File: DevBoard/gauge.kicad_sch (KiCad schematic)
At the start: 78 parts, among them J101 Pack (welded 4S) - use instea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, J102 Cell 1 NTC 10k 103AT, J103 EV2400 SMBus, J104 Bench PACK_P, J105 Cell 2 NTC 10k 103AT, J106 Cell 3 NTC 10k 103AT, J107 Cell 4 NTC 10k 103AT, Q101 AGM404AP1, Q102 AGM404AP1, Q103 AO3400A, Q104 AO3400A, SW101 WAKE, U101 BQ40Z50RSMR-R2, U102 BQ294700DSGR

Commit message: Dev board rev A7: CC2340R5MODA MCU, TMP1075 sensors, shared IRQ_N
- U301 STM32WB1MMC -> TI CC2340R5MODA (cost-down; BLE only, on-chip OTA).
  New symbol and footprint (MHA0024A, with the fig. 9-2 antenna keep-out),
  RF match C313/R321/C314/C315, RSTN pull-up R302, wired per SWRS349A fig. 9-1.
- Only 10 usable GPIOs, so the five board NTCs become TMP1075 I2C sensors:
  U302-U304 fitted (port 1 stage, port 2 stage, connectors), U305/U306 DNP.
  FET over-temperature moves to the gauge internal sensor.
- TPS25751 IRQs, gauge BTP and TMP1075 ALERTs share one open-drain IRQ_N
  (R314 pull-up; R315, R114 DNP).
- R313 fitted at 470k: CC2340 pins float in reset, so it keeps the 3V3 rail
  out of sleep mode during boot.
- Pin budget doc, circuit description, bring-up checklist and README item 40
  updated; mcu-io-power-states.md flagged for rewrite. PCB not updated yet.

Co-Authored-By: Claude Opus 5.5 <noreply@anthropic.com>
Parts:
- R114: now not fitted
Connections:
- net GAUGE_BTP renamed IRQ_N
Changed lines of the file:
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@@
 		)
 	)
-	(global_label "GAUGE_BTP"
+	(global_label "IRQ_N"
 		(shape bidirectional)
 		(at 294.64 181.61 270)
@@
 		)
 	)
-	(global_label "GAUGE_BTP"
+	(global_label "IRQ_N"
 		(shape bidirectional)
 		(at 312.42 190.5 270)
@@
 		)
 	)
-	(global_label "GAUGE_BTP"
+	(global_label "IRQ_N"
 		(shape bidirectional)
 		(at 342.9 179.07 90)
@@
 		(on_board yes)
 		(in_pos_files yes)
-		(dnp no)
+		(dnp yes)
 		(property "Reference" "R114"
 			(at 298.87 176.67 0)

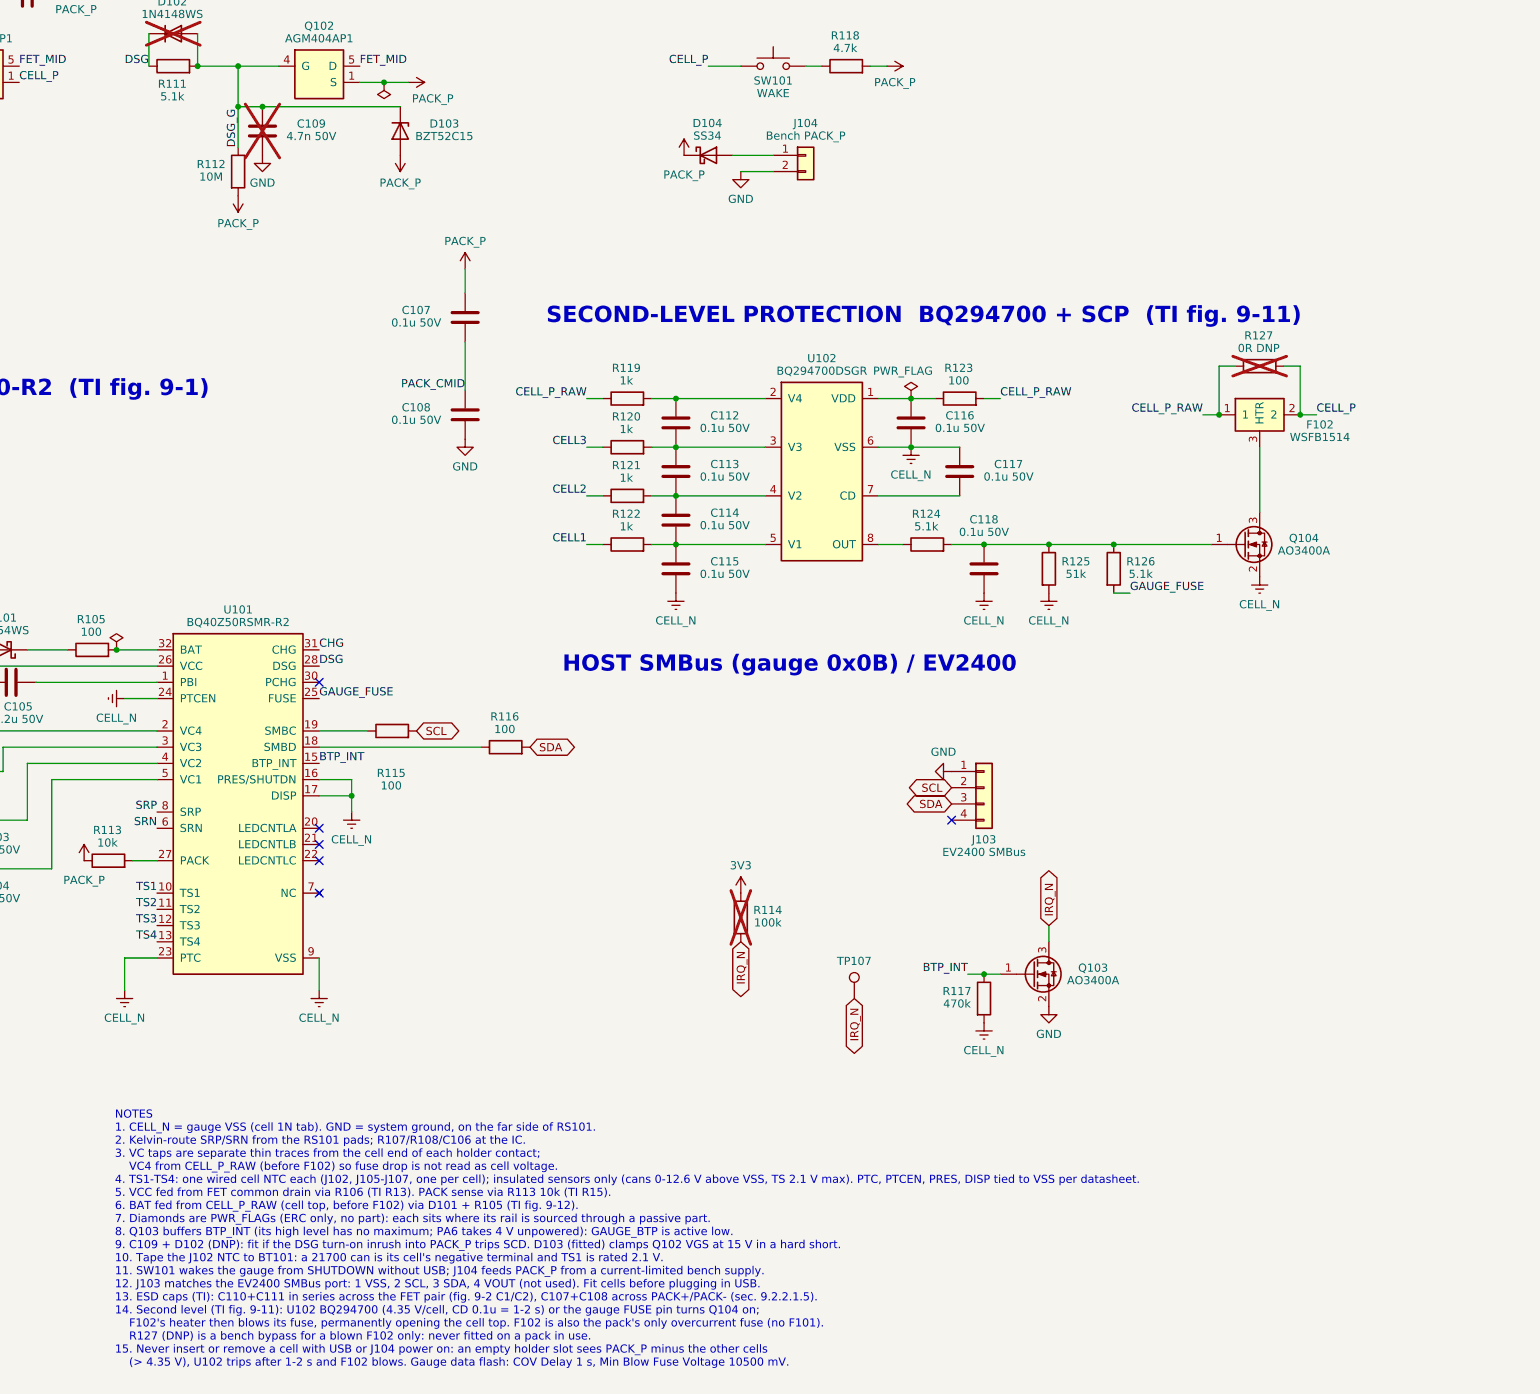
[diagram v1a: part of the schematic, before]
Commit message: Dev board rev A8 part 2: review 4 docs, BOM, A-2 procedure, J104 clamp
Schematic edits by tools/review4_docs.py (helpers split out of
review4_fixes.py into tools/sch_edit.py; review4_fixes output unchanged).
- A-2: EV2400 work only with 3V3 up (J104) and U301 in reset; checklist,
  R312/R301 Notes and MCU sheet note 10 rewritten.
- D-5: D105 SMAJ18A clamp on the J104 side of D104; board placed
  (D104 moved one body width left).
- Stale Notes, sheet notes, heading and address text fixed; sheet 4
  renamed "MCU and Sensors"; revision log A7/A8; title blocks A8.
- MPNs filled on the parts that had only LCSC numbers; Sourcing on U301
  and J301; J301 out of the position file.
- bringup-config-checklist, mcu-io-power-states and power-budget rewritten
  for the CC2340 with every review 4 CONFIG item; corrections in
  circuit-description, cost-down and cc2340-pin-budget.
ERC: 8 known warnings. 0 text overlaps. DRC: 0 parity issues, no
courtyard overlaps (429 parts). README item 42.

Co-Authored-By: Claude Opus 5.5 <noreply@anthropic.com>
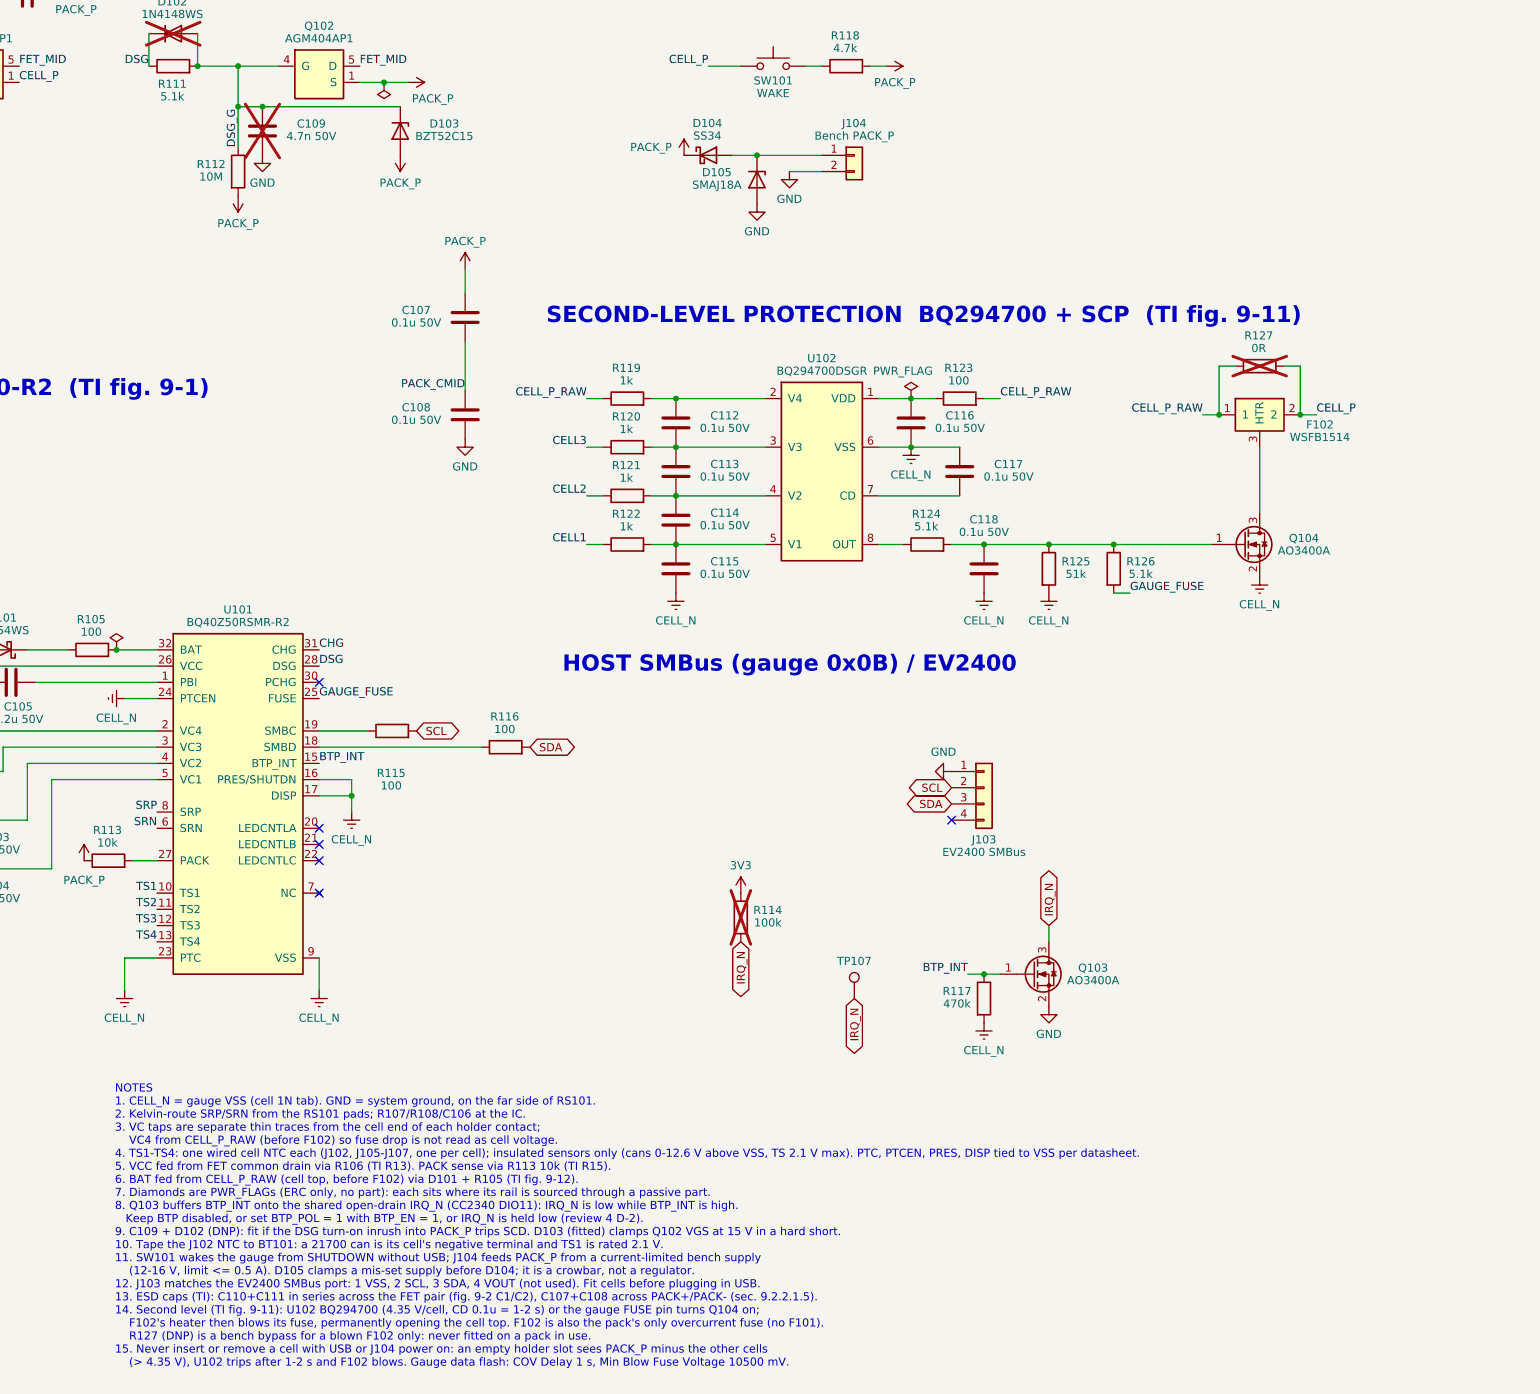
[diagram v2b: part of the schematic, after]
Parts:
- added D105: SMAJ18A, Diode_SMD:D_SMA, symbol Device:D_Zener
- BT101, BT102, BT103, BT104: MPN (none) -> BH-21700-B1BJ001 (MYOUNG)
- D101: MPN (none) -> BAT54WS (R+O)
- J102: Notes Wired 10k B3435 NTC (Semitec 103AT-2 class, epoxy bead with insulated leads) taped to the side of BT101, over its sleeve. The can is that cell's negative terminal (VSS above VSS) and the TS pins are rated 2.1 V: keep the sensor insulated. Gauge internal 18k pull-up; enable TS1 in data flash -> Wired 10k B3435 NTC (Semitec 103AT-2 class, epoxy bead with insulated leads) taped to the side of BT101, over its sleeve. The can is that cell's negative terminal (at VSS) and the TS pins are rated 2.1 V: keep the sensor insulated. Gauge internal 18k pull-up; enable TS1 in data flash
- Q101, Q102: MPN (none) -> AGM404AP1 (AGMSEMI)
- Q103: Notes BTP_INT level shift (inverts: GAUGE_BTP active low). AO3400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 -> BTP_INT level shift onto the shared open-drain IRQ_N (inver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
- R117: Notes Holds Q103 off when BTP_INT floats; 10-20 uA BTP source giv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 -> Holds Q103 off when BTP_INT floats (BTP_INT VOH is at most 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
- R127: value 0R DNP -> 0R
- RS101: MPN (none) -> PA2512FKE7W0R001E; Notes PA2512FKE7W0R001E -> 1 mOhm 1 % 2 W sense resistor (YAGEO)
- TP107: value GAUGE_BTP -> IRQ_N
- U101: MPN (none) -> BQ40Z50RSMR-R2
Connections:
- net GND: now also D105.2 (A)
- net at D104.2 (A), J104.1 (Pin_1): now also D105.1 (K)
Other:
- moved on the sheet: J104

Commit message: Dev board: cut JLC extended parts 37 -> 27 for a 2-board build
tools/bom_fee_cut.py (one-shot); README item 44. At 2 boards the costed
BOM goes from $124.28 to $108.49 per board.
- Basic/preferred swaps, no footprint changes: C313 -> C1548, C315/C314
  -> C1550, C401/C402 -> C1530 (X7R), R433/R434 -> 120k/22k 1 %
  (PP5V 5.16 V), C443/C543 -> 100 uF 35 V Honor polymer (same as C421).
- Hand-fit from LCSC: BT101-BT104, the 13 Harwin test loops, U202, D105
  (dev-only; out of the position file).
- Board: fields refreshed by netlist_to_board.py; also includes Logan's
  block move made in KiCad. DRC parity 0; ERC unchanged.

Co-Authored-By: Claude Opus 5.5 <noreply@anthropic.com>
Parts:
- BT101, BT102, BT103, BT104: LCSC C20606791 -> (none); Sourcing (none) -> Hand-solder, not JLC assembled (dev-only 21700 holder; save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
- D105: LCSC C148219 -> (none); Sourcing (none) -> Hand-solder, not JLC assembled (dev-only bench-input clamp;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
- TP109: LCSC C55121754 -> (none); Sourcing (none) -> Hand-solder, not JLC assembled (test loop, dev only; saves 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
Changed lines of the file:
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@@
 		(in_bom yes)
 		(on_board yes)
-		(in_pos_files yes)
+		(in_pos_files no)
 		(dnp no)
 		(property "Reference" "BT101"
@@
 			)
 		)
-		(property "LCSC" "C20606791"
+		(property "LCSC" ""
 			(at 38.1 139.7 0)
 			(hide yes)
@@
 			)
 		)
+		(property "Sourcing" "Hand-solder, not JLC assembled (dev-only 21700 holder; saves a JLC extended-part fee; LCSC C20606791 BH-21700-B1BJ001 (MYOUNG))"
+			(at 38.1 139.7 0)
+			(hide yes)
+			(show_name no)
+			(do_not_autoplace no)
+			(effects
+				(font
+					(size 1.27 1.27)
+				)
+			)
+		)
 		(pin "1"
 		)
@@
 		(in_bom yes)
 		(on_board yes)
-		(in_pos_files yes)
+		(in_pos_files no)
 		(dnp no)
 		(property "Reference" "BT102"
@@
 			)
 		)
-		(property "LCSC" "C20606791"
+		(property "LCSC" ""
 			(at 38.1 114.3 0)
 			(hide yes)
@@
 			)
 		)
+		(property "Sourcing" "Hand-solder, not JLC assembled (dev-only 21700 holder; saves a JLC extended-part fee; LCSC C20606791 BH-21700-B1BJ001 (MYOUNG))"
+			(at 38.1 114.3 0)
+			(hide yes)
+			(show_name no)
+			(do_not_autoplace no)
+			(effects
+				(font
+					(size 1.27 1.27)
+				)
+			)
+		)
 		(pin "1"
 		)
@@
 		(in_bom yes)
 		(on_board yes)
-		(in_pos_files yes)
+		(in_pos_files no)
 		(dnp no)
 		(property "Reference" "BT104"
@@
 			)
 		)
-		(property "LCSC" "C20606791"
+		(property "LCSC" ""
 			(at 38.1 63.5 0)
 			(hide yes)
@@
 			)
 		)
+		(property "Sourcing" "Hand-solder, not JLC assembled (dev-only 21700 holder; saves a JLC extended-part fee; LCSC C20606791 BH-21700-B1BJ001 (MYOUNG))"
+			(at 38.1 63.5 0)
+			(hide yes)
+			(show_name no)
+			(do_not_autoplace no)
+			(effects
+				(font
+					(size 1.27 1.27)
+				)
+			)
+		)
 		(pin "1"
 		)
@@
 		(in_bom yes)
 		(on_board yes)
-		(in_pos_files yes)
+		(in_pos_files no)
 		(dnp no)
 		(property "Reference" "BT103"
@@
 			)
 		)
-		(property "LCSC" "C20606791"
+		(property "LCSC" ""
 			(at 38.1 88.9 0)
 			(hide yes)
@@
 			)
 		)
+		(property "Sourcing" "Hand-solder, not JLC assembled (dev-only 21700 holder; saves a JLC extended-part fee; LCSC C20606791 BH-21700-B1BJ001 (MYOUNG))"
+			(at 38.1 88.9 0)
+			(hide yes)
+			(show_name no)
+			(do_not_autoplace no)
+			(effects
+				(font
+					(size 1.27 1.27)
+				)
+			)
+		)
 		(pin "1"
 		)
@@
 		(in_bom yes)
 		(on_board yes)
-		(in_pos_files yes)
+		(in_pos_files no)
 		(dnp no)
 		(property "Reference" "TP109"
@@
 			)
 		)
-		(property "LCSC" "C55121754"
+		(property "LCSC" ""
 			(at 137.16 264.16 0)
 			(hide yes)
@@
 			)
 		)
+		(property "Sourcing" "Hand-solder, not JLC assembled (test loop, dev only; saves a JLC extended-part fee; LCSC C55121754 RH-S2761-46R (ronghe; Harwin S2761-46R equivalent))"
+			(at 137.16 264.16 0)
+			(hide yes)
+			(show_name no)
+			(do_not_autoplace no)
+			(effects
+				(font
+					(size 1.27 1.27)
+				)
+			)
+		)
 		(pin "1"
 		)
@@
 		(in_bom yes)
 		(on_board yes)
-		(in_pos_files yes)
+		(in_pos_files no)
 		(dnp no)
 		(property "Reference" "D105"
@@
 			)
 		)
-		(property "LCSC" "C148219"
+		(property "LCSC" ""
 			(at 297.18 62.23 0)
 			(hide yes)
@@
 			(at 297.18 62.23 0)
 			(hide yes)
+			(show_name no)
+			(do_not_autoplace no)
+			(effects
+				(font
+					(size 1.27 1.27)
+				)
+			)
+		)
+		(property "Sourcing" "Hand-solder, not JLC assembled (dev-only bench-input clamp; saves a JLC extended-part fee; LCSC C148219 SMAJ18A (Littelfuse))"
+			(at 297.18 62.23 0)
+			(hide yes)

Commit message: Dev board: downsize passives to 0402 where basic parts allow
160 resistors and capacitors move to the smallest package that keeps their
rating: never below 0402, and no JLC basic part becomes extended. Connectivity
and ERC are unchanged, extended parts stay at 27, and the cost goes from
$108.49 to $107.93 per board at 2 boards. Applied by
tools/downsize_passives.py (one-shot); README item 45 lists what moved, what
stayed and why. The PCB still needs Update PCB from Schematic.

Co-Authored-By: Claude Opus 5.5 <noreply@anthropic.com>
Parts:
- C101, C102, C103, C104, C106, C107, C108, C110, C111, C112, C113, C114, C115, C116, C117, C118: footprint Capacitor_SMD:C_0603_1608Metric -> Capacitor_SMD:C_0402_1005Metric; LCSC C14663 -> C307331; MPN CC0603KRX7R9BB104 -> CL05B104KB54PNC
- C105: footprint Capacitor_SMD:C_1206_3216Metric -> Capacitor_SMD:C_0805_2012Metric; LCSC C50254 -> C377773; MPN CL31B225KBHNNNE -> CL21A225KBQNNNE
- R105, R106, R107, R108, R115, R116, R123: footprint Resistor_SMD:R_0603_1608Metric -> Resistor_SMD:R_0402_1005Metric; LCSC C22775 -> C25076; MPN 0603WAF1000T5E -> 0402WGF1000TCE
- R109, R111, R124, R126: footprint Resistor_SMD:R_0603_1608Metric -> Resistor_SMD:R_0402_1005Metric; LCSC C23186 -> C25905; MPN 0603WAF5101T5E -> 0402WGF5101TCE
- R113: footprint Resistor_SMD:R_0603_1608Metric -> Resistor_SMD:R_0402_1005Metric; LCSC C25804 -> C25744; MPN 0603WAF1002T5E -> 0402WGF1002TCE
- R114: footprint Resistor_SMD:R_0603_1608Metric -> Resistor_SMD:R_0402_1005Metric; LCSC C25803 -> C25741; MPN 0603WAF1003T5E -> 0402WGF1003TCE
- R118: footprint Resistor_SMD:R_0603_1608Metric -> Resistor_SMD:R_0402_1005Metric; LCSC C23162 -> C25900; MPN 0603WAF4701T5E -> 0402WGF4701TCE
- R119, R120, R121, R122: footprint Resistor_SMD:R_0603_1608Metric -> Resistor_SMD:R_0402_1005Metric; LCSC C21190 -> C11702; MPN 0603WAF1001T5E -> 0402WGF1001TCE
- R125: footprint Resistor_SMD:R_0603_1608Metric -> Resistor_SMD:R_0402_1005Metric; LCSC C23196 -> C25794; MPN 0603WAF5102T5E -> 0402WGF5102TCE
